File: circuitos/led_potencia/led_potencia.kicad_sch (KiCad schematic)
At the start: 67 parts, among them J1 Conn_01x02_Pin, J10 Conn_01x02_Pin, J11 Conn_01x02_Pin, J12 Conn_01x02_Pin, J13 Conn_01x02_Pin, J14 Conn_01x02_Pin, J15 Conn_01x02_Pin, J16 Conn_01x02_Pin, J17 Conn_01x02_Socket, J19 Conn_01x02_OE_GND, J2 Conn_01x02_Pin, J20 Conn_01x05_IN, J21 Conn_01x05_OUT, J3 Conn_01x02_Pin, J4 Conn_01x02_Pin, J5 Conn_01x02_Pin, J6 Conn_01x02_Pin, J7 Conn_01x02_Pin, J8 Conn_01x02_Pin, J9 Conn_01x02_Pin, Q1 IRLZ44N, Q18 IRF4905, Q19 IRF4905, Q2 IRLZ44N, Q20 IRF4905, Q21 PN2222A, Q22 PN2222A, Q23 PN2222A, Q24 IRF4905, Q25 PN2222A, Q3 IRLZ44N, Q4 IRLZ44N, U1 74HC595

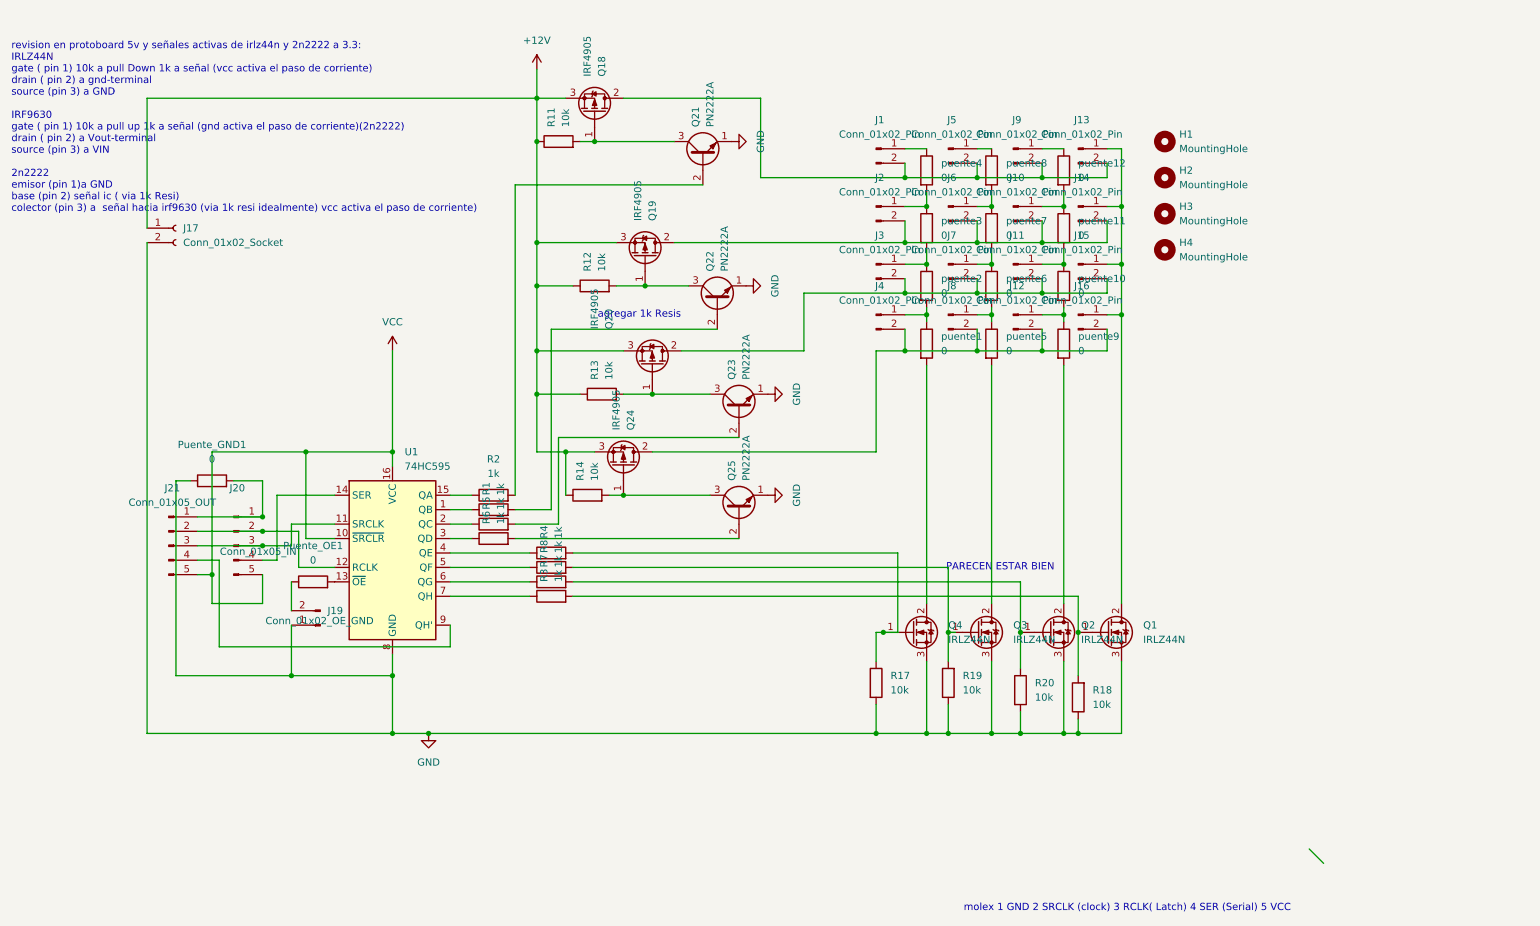
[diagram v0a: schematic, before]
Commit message: cambio irlz44n x8x2 subida pre simplificar
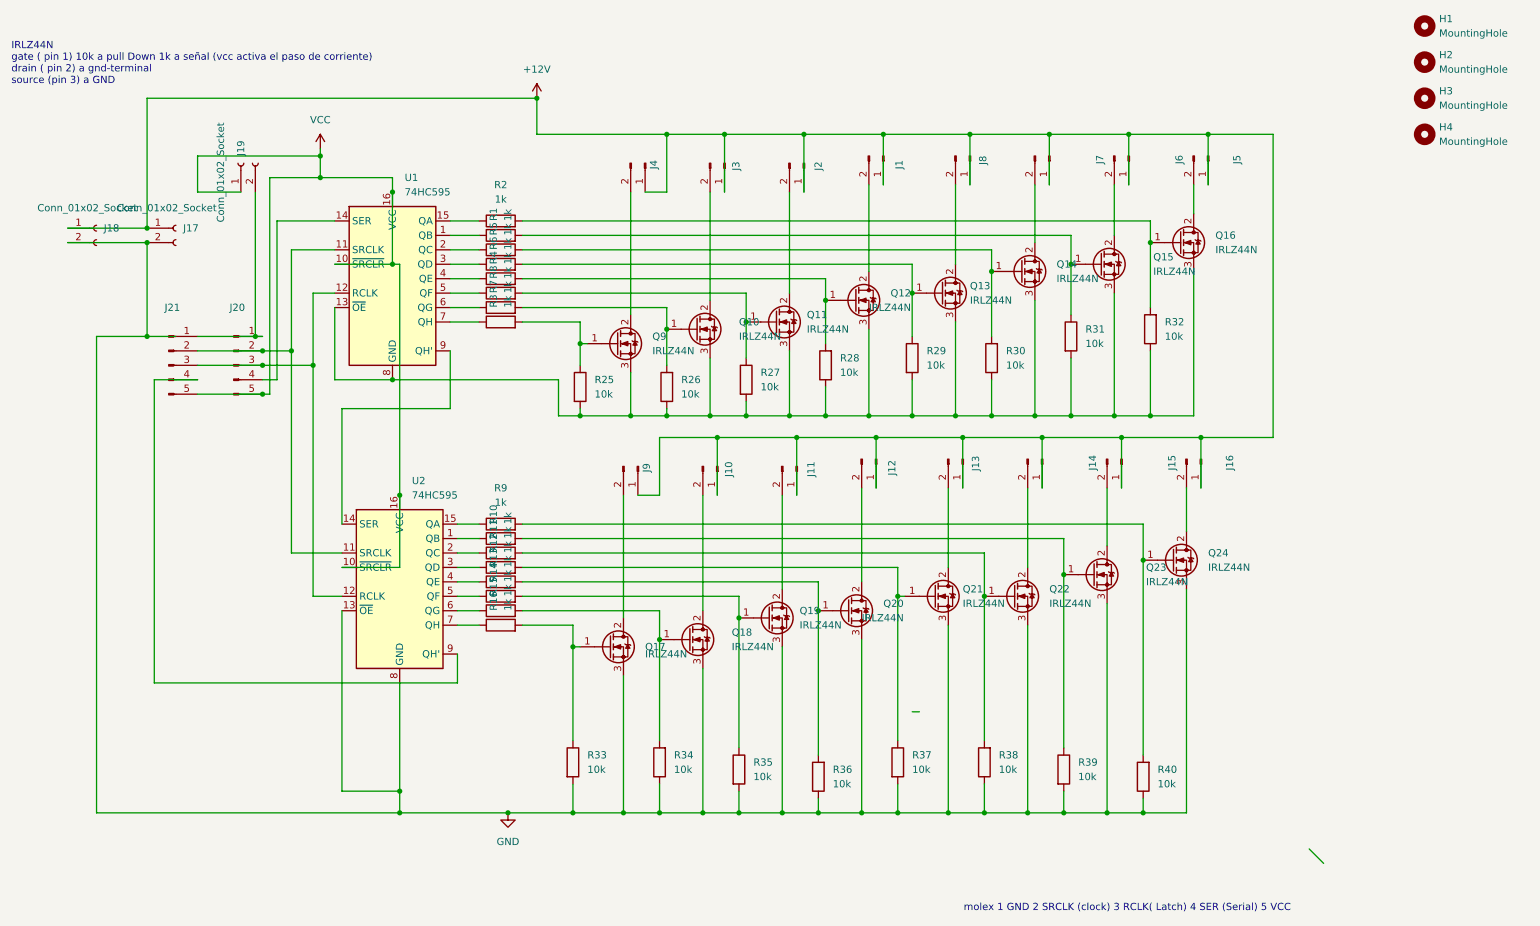
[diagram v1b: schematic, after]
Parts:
- removed J19: Conn_01x02_OE_GND, Connector_Molex:Molex_KK-254_AE-6410-02A_1x02_P2.54mm_Vertical, symbol Connector:Conn_01x02_Pin
- removed Puente_GND1: 0, Resistor_THT:R_Axial_DIN0207_L6.3mm_D2.5mm_P10.16mm_Horizontal, symbol Device:R
- removed Puente_OE1, puente1, puente10, puente11, puente12, puente2, puente3, puente4, puente5, puente6, puente7, puente8, puente9: 0, Resistor_THT:R_Axial_DIN0204_L3.6mm_D1.6mm_P5.08mm_Horizontal, symbol Device:R
- removed Q1, Q2, Q3, Q4: IRLZ44N, Package_TO_SOT_THT:TO-220-3_Vertical, symbol Transistor_FET:IRLZ44N
- removed Q18, Q19, Q20, Q24: IRF4905, Package_TO_SOT_THT:TO-220-3_Vertical, symbol Transistor_FET:IRF4905
- removed Q21, Q22, Q23, Q25: PN2222A, Package_TO_SOT_THT:TO-92_Inline, symbol Transistor_BJT:PN2222A
- removed R17, R18, R19, R20: 10k, Resistor_THT:R_Axial_DIN0204_L3.6mm_D1.6mm_P7.62mm_Horizontal, symbol Device:R
- added J18, J19: Conn_01x02_Socket, Connector_Molex:Molex_KK-254_AE-6410-02A_1x02_P2.54mm_Vertical, symbol Connector:Conn_01x02_Socket
- added Q10, Q11, Q12, Q13, Q14, Q15, Q16, Q17, Q18, Q19, Q20, Q21, Q22, Q23, Q24, Q9: IRLZ44N, Package_TO_SOT_THT:TO-220-3_Vertical, symbol Transistor_FET:IRLZ44N
- added R10, R15, R16, R9: 1k, Resistor_THT:R_Axial_DIN0204_L3.6mm_D1.6mm_P7.62mm_Horizontal, symbol Device:R
- added R25, R26, R27, R28, R29, R30, R31, R32, R33, R34, R35, R36, R37, R38, R39, R40: 10k, Resistor_THT:R_Axial_DIN0204_L3.6mm_D1.6mm_P7.62mm_Horizontal, symbol Device:R
- added U2: 74HC595, Package_DIP:DIP-16_W7.62mm_Socket_LongPads, symbol 74xx:74HC595
- R11, R12, R13, R14: value 10k -> 1k
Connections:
- net +12V: now also J1.1 (Pin_1), J10.1 (Pin_1), J11.1 (Pin_1), J12.1 (Pin_1), J13.1 (Pin_1), J14.1 (Pin_1), J15.1 (Pin_1), J16.1 (Pin_1), J2.1 (Pin_1), J3.1 (Pin_1), J4.1 (Pin_1), J5.1 (Pin_1), J6.1 (Pin_1), J7.1 (Pin_1), J8.1 (Pin_1), J9.1 (Pin_1), J18.1 (Pin_1); no longer R11.1, R12.1, R13.1, R14.1
- net GND: now also J18.2 (Pin_2), Q17.3 (S), Q18.3 (S), Q19.3 (S), Q20.3 (S), Q21.3 (S), Q22.3 (S), Q23.3 (S), Q24.3 (S), R33.2, R34.1, R35.2, R36.1, R37.2, R38.1, R39.2, R40.1, U2.13 (~{OE}), U2.8 (GND); no longer U1.8 (GND)
- net VCC: now also J19.1 (Pin_1), U2.10 (~{SRCLR}), U2.16 (VCC)
- net at R5.2: now also Q14.1 (G), R30.2
- net at R13.2: now also Q20.1 (G), R36.2
- net at R12.2: now also Q21.1 (G), R37.1
- net at R14.2: now also Q19.1 (G), R35.1
- net at R11.2: now also Q22.1 (G), R38.2
- net at J20.1 (Pin_1), J21.1 (Pin_1): now also J19.2 (Pin_2)
- net at J20.2 (Pin_2), J21.2 (Pin_2): now also U1.11 (SRCLK), U2.11 (SRCLK); no longer U1.12 (RCLK)
- net at J20.3 (Pin_3), J21.3 (Pin_3): now also U1.12 (RCLK), U2.12 (RCLK); no longer U1.11 (SRCLK)
- net at J21.4 (Pin_4): now also U2.9 (QH'); no longer U1.9 (QH')
- net at R6.2: now also Q13.1 (G), R29.1
- net at R8.2: now also Q11.1 (G), R27.1
- net at R2.2: now also Q16.1 (G), R32.2
- net at R3.2: now also Q9.1 (G), R25.1
- net at R4.2: now also Q12.1 (G), R28.2
- net at R7.2: now also Q10.1 (G), R26.2
- net at U1.13 (~{OE}): now also U1.8 (GND), Q10.3 (S), Q11.3 (S), Q12.3 (S), Q13.3 (S), Q14.3 (S), Q15.3 (S), Q16.3 (S), Q9.3 (S), R25.2, R26.1, R27.2, R28.1, R29.2, R30.1, R31.2, R32.1
- net at R1.2: now also Q15.1 (G), R31.1
- new net: R14.1, U2.5 (QF)
- new net: J9.2 (Pin_2), Q17.2 (D)
- new net: R15.1, U2.6 (QG)
- new net: Q18.1 (G), R15.2, R34.2
- new net: Q23.1 (G), R10.2, R39.1
- new net: J15.2 (Pin_2), Q23.2 (D)
- new net: R9.1, U2.15 (QA)
- new net: Q24.1 (G), R40.2, R9.2
- new net: R11.1, U2.2 (QC)
- new net: J7.2 (Pin_2), Q14.2 (D)
- new net: J4.2 (Pin_2), Q9.2 (D)
- new net: J11.2 (Pin_2), Q19.2 (D)
- new net: R12.1, U2.3 (QD)
- new net: J10.2 (Pin_2), Q18.2 (D)
- new net: J1.2 (Pin_2), Q12.2 (D)
- new net: R16.1, U2.7 (QH)
- new net: Q17.1 (G), R16.2, R33.1
- new net: J5.2 (Pin_2), Q16.2 (D)
- new net: R10.1, U2.1 (QB)
- new net: J12.2 (Pin_2), Q20.2 (D)
- new net: J3.2 (Pin_2), Q10.2 (D)
- new net: J2.2 (Pin_2), Q11.2 (D)
- new net: R13.1, U2.4 (QE)
- new net: U1.9 (QH'), U2.14 (SER)
- new net: J6.2 (Pin_2), Q15.2 (D)
- new net: J14.2 (Pin_2), Q22.2 (D)
- new net: J13.2 (Pin_2), Q21.2 (D)
- new net: J8.2 (Pin_2), Q13.2 (D)
- new net: J16.2 (Pin_2), Q24.2 (D)
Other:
- note added: "IRLZ44N gate ( pin 1) 10k a pull Down 1k a señal (vcc activa el paso de corriente) drain ( pin 2) a gnd-terminal source (pin 3) a GND"
- note removed: "PARECEN ESTAR BIEN"
- note removed: "agregar 1k Resis"
- note removed: "revision en protoboard 5v y señales activas de irlz44n y 2n2222 a 3.3: IRLZ44N gate ( pin 1) 10k a pull Down 1k a señal (vcc activa el paso de corriente) drain ( pin 2) a gnd-terminal source (pin 3) a GND IRF9630 gate ( pin 1) 10k a pull up 1k a señal (gnd activa el paso de corriente)(2n2222) drain ( pin 2) a Vout-terminal source (pin 3) a VIN 2n2222 emisor (pin 1)a GND base (pin 2) señal ic ( vi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"
- moved on the sheet: H1, H2, H3, H4, J1, J2, J20, J21, J3, J4, J5, J6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

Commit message: simplificacion juegos de 1 ic x pcb 8 irlzn
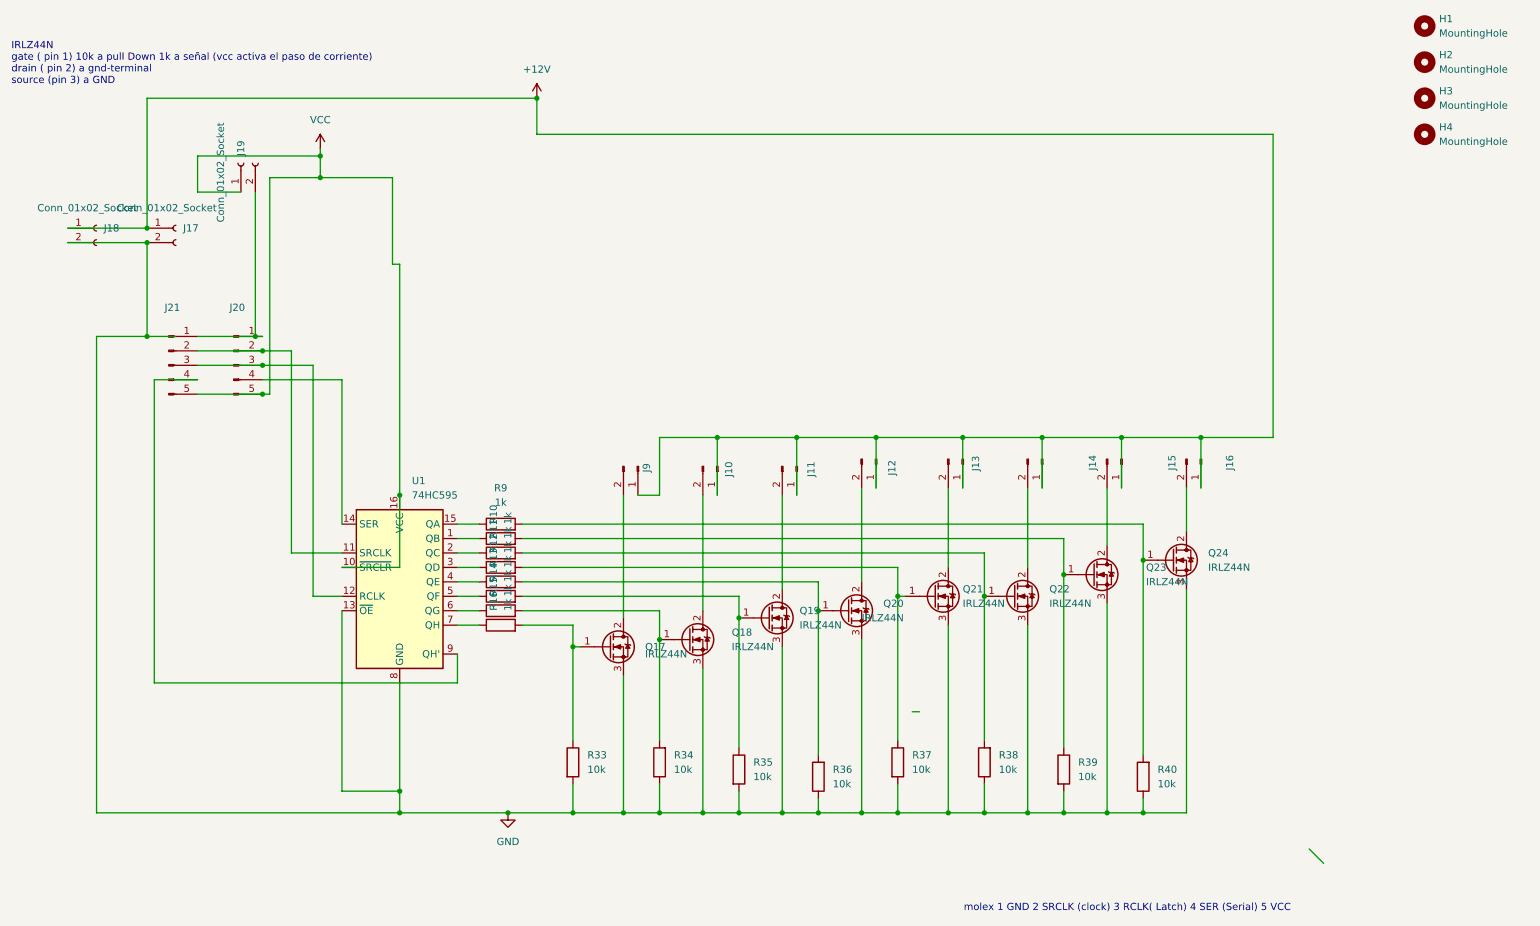
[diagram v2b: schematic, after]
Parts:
- removed J1, J2, J3, J4, J5, J6, J7, J8: Conn_01x02_Pin, Connector_Molex:Molex_KK-254_AE-6410-02A_1x02_P2.54mm_Vertical, symbol Connector:Conn_01x02_Pin
- removed Q10, Q11, Q12, Q13, Q14, Q15, Q16, Q9: IRLZ44N, Package_TO_SOT_THT:TO-220-3_Vertical, symbol Transistor_FET:IRLZ44N
- removed R1, R2, R3, R4, R5, R6, R7, R8: 1k, Resistor_THT:R_Axial_DIN0204_L3.6mm_D1.6mm_P7.62mm_Horizontal, symbol Device:R
- removed R25, R26, R27, R28, R29, R30, R31, R32: 10k, Resistor_THT:R_Axial_DIN0204_L3.6mm_D1.6mm_P7.62mm_Horizontal, symbol Device:R
- removed U1: 74HC595, Package_DIP:DIP-16_W7.62mm_Socket_LongPads, symbol 74xx:74HC595
- renumbered U2 to U1
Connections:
- net at J20.4 (Pin_4): now also U1.14 (SER)

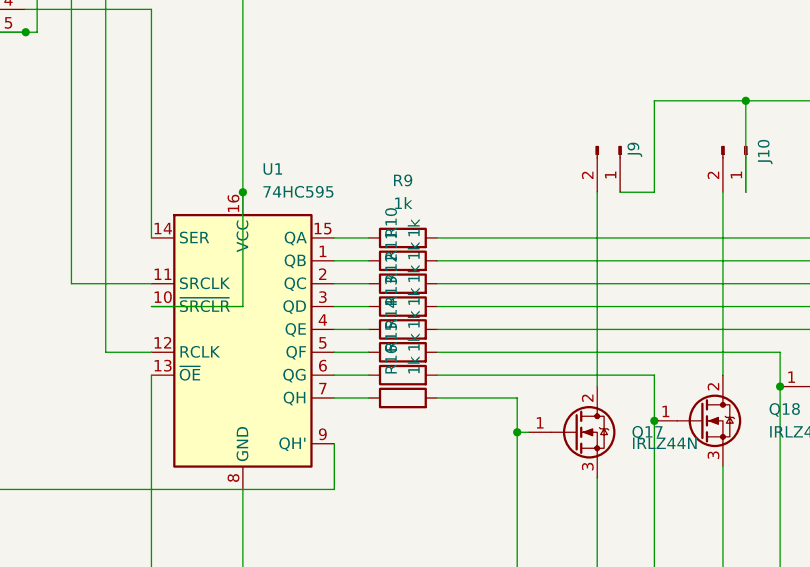
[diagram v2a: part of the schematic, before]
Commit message: cambiando resistencias
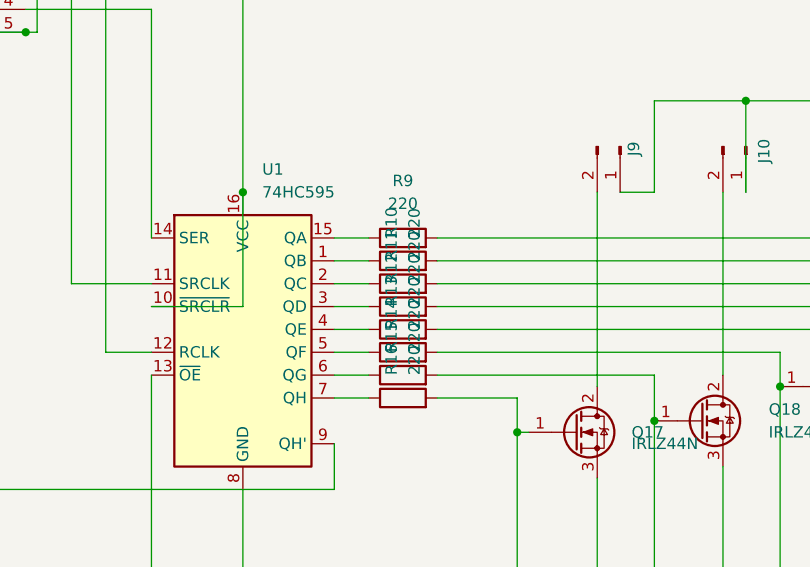
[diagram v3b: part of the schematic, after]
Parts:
- R10, R11, R12, R13, R14, R15, R16, R9: value 1k -> 220

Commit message: cambiando resistencias
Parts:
- added J1, J2: Conn_01x03_Pin, Connector_Molex:Molex_KK-254_AE-6410-03A_1x03_P2.54mm_Vertical, symbol Connector:Conn_01x03_Pin
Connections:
- net at J20.2 (Pin_2), J21.2 (Pin_2), U1.11 (SRCLK): now also J1.1 (Pin_1), J2.1 (Pin_1)
- net at J20.3 (Pin_3), J21.3 (Pin_3), U1.12 (RCLK): now also J1.2 (Pin_2), J2.2 (Pin_2)
- net at J21.4 (Pin_4), U1.9 (QH'): now also J1.3 (Pin_3)
- net at J20.4 (Pin_4), U1.14 (SER): now also J2.3 (Pin_3)

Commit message: ruteo : pre inversion
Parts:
- removed J20: Conn_01x05_IN, Connector_Molex:Molex_KK-254_AE-6410-05A_1x05_P2.54mm_Vertical, symbol Connector:Conn_01x05_Pin
- removed J21: Conn_01x05_OUT, Connector_Molex:Molex_KK-254_AE-6410-05A_1x05_P2.54mm_Vertical, symbol Connector:Conn_01x05_Pin
- added J3: Conn_01x02_Socket, Connector_Molex:Molex_KK-254_AE-6410-02A_1x02_P2.54mm_Vertical, symbol Connector:Conn_01x02_Socket
- added puente: 0, Resistor_THT:R_Axial_DIN0204_L3.6mm_D1.6mm_P7.62mm_Horizontal, symbol Device:R
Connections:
- net +12V: now also J17.2 (Pin_2), J18.2 (Pin_2); no longer J17.1 (Pin_1), J18.1 (Pin_1)
- net GND: now also J17.1 (Pin_1), J18.1 (Pin_1), J19.1 (Pin_1), J3.1 (Pin_1), puente.1, puente.2; no longer J17.2 (Pin_2), J18.2 (Pin_2)
- net VCC: now also J19.2 (Pin_2), J3.2 (Pin_2); no longer J19.1 (Pin_1)
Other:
- moved on the sheet: J17, J18

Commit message: ruteo : pre inversion
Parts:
- renumbered puente to puente1
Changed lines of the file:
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@@
 		(dnp no)
 		(fields_autoplaced yes)
-		(property "Reference" "puente"
+		(property "Reference" "puente1"
 			(at 96.52 140.9699 0)
 			(show_name no)
@@
 			(project "led_potencia"
 				(path "/f9546c60-e06e-4d9b-9eb6-79a4ed645b82"
-					(reference "puente")
+					(reference "puente1")
 					(unit 1)
 				)
